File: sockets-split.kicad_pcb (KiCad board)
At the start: 2 copper layers, 63 parts, among them J2 MJ-4PP-9, P1 i2c-pin, P2 i2c-pin, SW1 RESET_SW, SW10 SW_PUSH, SW11 SW_PUSH, SW12 SW_PUSH, SW13 SW_PUSH, SW14 SW_PUSH, SW15 SW_PUSH, SW16 SW_PUSH, SW17 SW_PUSH, SW18 SW_PUSH, SW19 SW_PUSH, SW2 SW_PUSH, SW20 SW_PUSH, SW21 SW_PUSH, SW22 SW_PUSH, SW23 SW_PUSH, SW24 SW_PUSH, SW25 SW_PUSH, SW3 SW_PUSH, SW4 SW_PUSH, SW5 SW_PUSH, SW6 SW_PUSH, SW7 SW_PUSH, SW8 SW_PUSH, SW9 SW_PUSH, U1 ProMicro

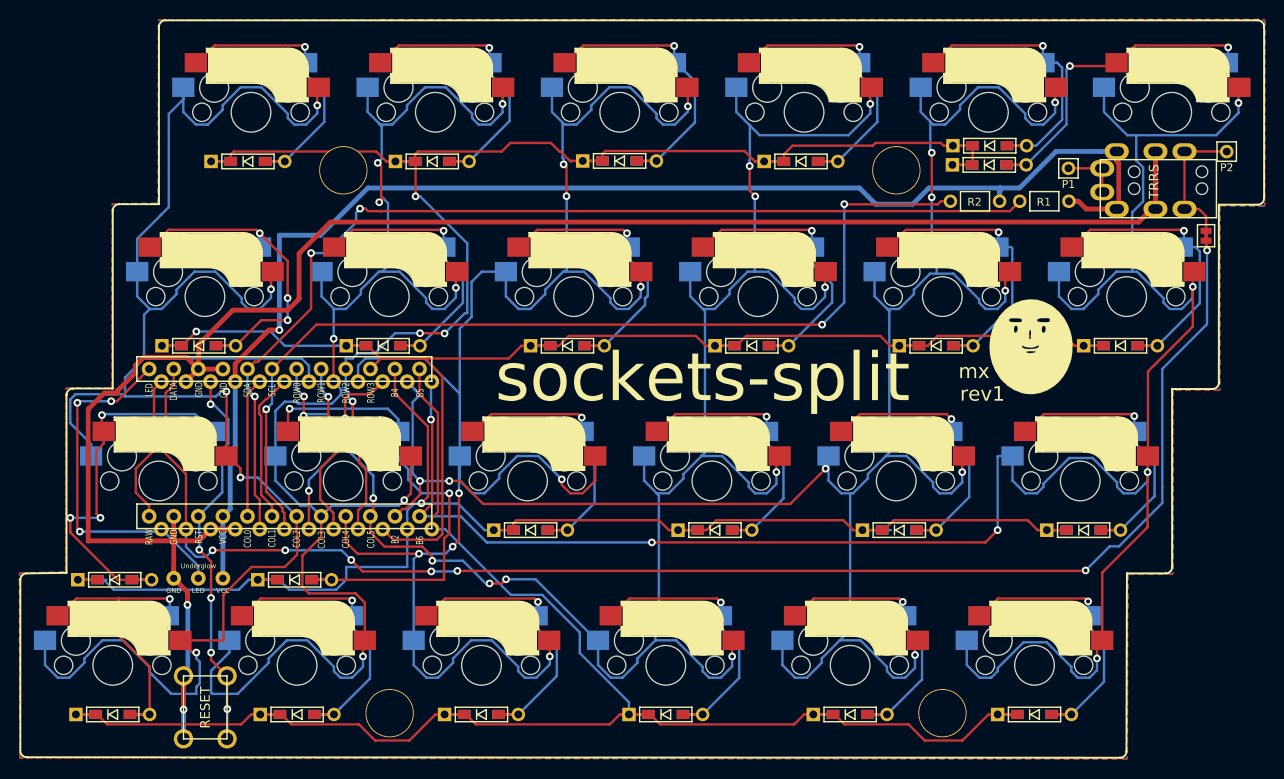
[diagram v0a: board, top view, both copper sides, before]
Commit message: Fix module & draw case line
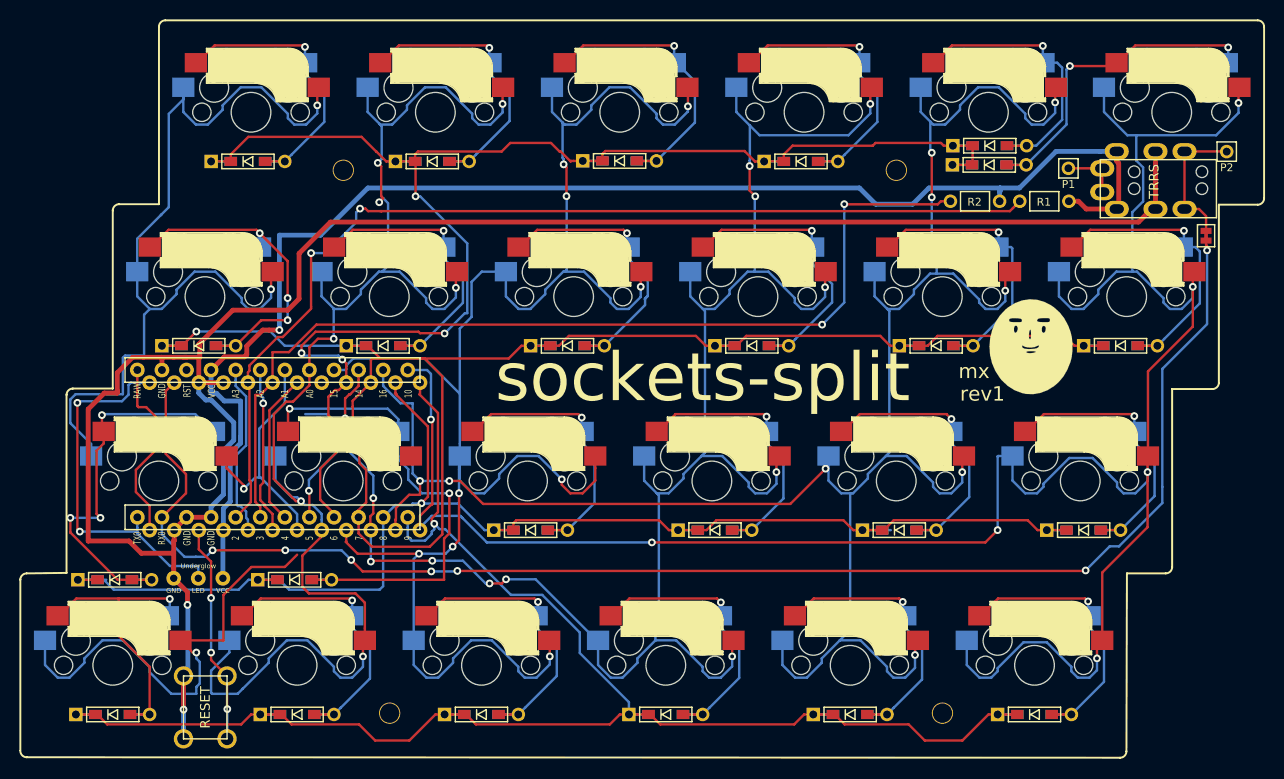
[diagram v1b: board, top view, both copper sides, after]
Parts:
- removed Ref** (x4): Val**, kbd:HOLE
- added ?: , kbd:HOLE_M2, F.Cu at (124.4, 67.8)
- added ?: , kbd:HOLE_M2, F.Cu at (181.9, 67.7)
- added ?: , kbd:HOLE_M2, F.Cu at (186.3, 124.1)
- added ?: , kbd:HOLE_M2, F.Cu at (129.4, 124.5)
- U1: footprint kbd:ProMicro_v2 -> kbd:ProMicro_v2_ura_pcb_for_sockets_split
- moved U1 1.22 mm to (117.6, 95.8)
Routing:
- net col0: track 191.0 -> 166.8 mm, vias 5 -> 4
- net row1: track 142.0 -> 164.6 mm
- net RESET: track 40.4 -> 22.8 mm, vias 5 -> 3
- net GND: track 189.3 -> 205.7 mm
- net row0: track 153.1 -> 163.4 mm
- net col1: track 158.5 -> 148.5 mm
- net VCC: track 142.8 -> 148.7 mm
- net col5: track 231.0 -> 236.7 mm
- net Net-(U1-Pad7): track 21.1 -> 15.8 mm, vias 3 -> 0
- net Net-(U1-Pad24): track 15.6 -> 20.4 mm
- net row3: track 164.4 -> 168.6 mm, vias 0 -> 1
- net col4: track 204.6 -> 208.8 mm
- net Net-(U1-Pad8): track 18.4 -> 14.5 mm
- net Net-(U1-Pad20): track 14.4 -> 18.0 mm
- net Net-(U1-Pad19): track 15.6 -> 17.3 mm, vias 0 -> 1
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- removed copper zone on B.Cu, net GND
- removed copper zone on F.Cu, net GND

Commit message: Fix promicro, case
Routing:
- net GND: track 205.7 -> 205.0 mm
- added copper zone on B.Cu, net GND
- added copper zone on F.Cu, net GND
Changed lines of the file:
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@@
     (thickness 1.6)
     (drawings 161)
-    (tracks 1485)
+    (tracks 1492)
     (zones 0)
     (modules 63)
@@
     (0 F.Cu signal)
     (31 B.Cu signal)
-    (32 B.Adhes user)
-    (33 F.Adhes user)
-    (34 B.Paste user)
-    (35 F.Paste user)
+    (32 B.Adhes user hide)
+    (33 F.Adhes user hide)
+    (34 B.Paste user hide)
+    (35 F.Paste user hide)
     (36 B.SilkS user)
     (37 F.SilkS user)
@@
     (39 F.Mask user)
     (40 Dwgs.User user)
-    (41 Cmts.User user)
-    (42 Eco1.User user)
-    (43 Eco2.User user)
-    (44 Edge.Cuts user)
-    (45 Margin user)
-    (46 B.CrtYd user)
+    (41 Cmts.User user hide)
+    (42 Eco1.User user hide)
+    (43 Eco2.User user hide)
+    (44 Edge.Cuts user hide)
+    (45 Margin user hide)
+    (46 B.CrtYd user hide)
     (47 F.CrtYd user hide)
-    (48 B.Fab user)
-    (49 F.Fab user)
+    (48 B.Fab user hide)
+    (49 F.Fab user hide)
   )
   (setup
@@
     (visible_elements 7FFFE7FF)
     (pcbplotparams
-      (layerselection 0x00100_7ffffffe)
+      (layerselection 0x010f0_ffffffff)
       (usegerberextensions false)
       (usegerberattributes false)
@@
       (padsonsilk false)
       (subtractmaskfromsilk false)
-      (outputformat 3)
+      (outputformat 1)
       (mirror false)
       (drillshape 0)
@@
   (segment (start 102.5622 109.7788) (end 104.5972 109.7788) (width 0.25) (layer B.Cu) (net 15))
   (segment (start 102.5622 109.7788) (end 104.5972 109.7788) (width 0.25) (layer F.Cu) (net 15))
-  (via (at 96.2014 103.378) (size 0.8) (drill 0.4) (layers F.Cu B.Cu) (net 15))
-  (segment (start 96.2014 104.894402) (end 96.2014 103.378) (width 0.25) (layer F.Cu) (net 15))
-  (via (at 99.314 103.378) (size 0.8) (drill 0.4) (layers F.Cu B.Cu) (net 15))
-  (segment (start 96.2014 103.378) (end 99.314 103.378) (width 0.25) (layer B.Cu) (net 15))
+  (via (at 97.3328 103.378) (size 0.8) (drill 0.4) (layers F.Cu B.Cu) (net 15))
+  (via (at 100.584 103.378) (size 0.8) (drill 0.4) (layers F.Cu B.Cu) (net 15))
+  (segment (start 97.4344 103.378) (end 100.547 103.378) (width 0.25) (layer B.Cu) (net 15))
   (segment (start 99.6465 95.698) (end 99.6465 94.448) (width 0.25) (layer F.Cu) (net 15))
   (segment (start 98.914001 96.430499) (end 99.6465 95.698) (width 0.25) (layer F.Cu) (net 15))
-  (segment (start 98.914001 102.978001) (end 98.914001 96.430499) (width 0.25) (layer F.Cu) (net 15))
-  (segment (start 99.314 103.378) (end 98.914001 102.978001) (width 0.25) (layer F.Cu) (net 15))
-  (segment (start 96.2014 104.894402) (end 96.207602 104.894402) (width 0.25) (layer F.Cu) (net 15))
   (segment (start 101.092 109.7788) (end 102.5622 109.7788) (width 0.25) (layer F.Cu) (net 15))
-  (segment (start 96.207602 104.894402) (end 101.092 109.7788) (width 0.25) (layer F.Cu) (net 15))
+  (segment (start 98.914001 100.5332) (end 99.472801 101.092) (width 0.25) (layer F.Cu) (net 15))
+  (segment (start 98.914001 100.5332) (end 98.914001 96.430499) (width 0.25) (layer F.Cu) (net 15))
+  (segment (start 99.472801 101.092) (end 100.0252 101.092) (width 0.25) (layer F.Cu) (net 15))
+  (segment (start 100.584 101.6508) (end 100.584 103.378) (width 0.25) (layer F.Cu) (net 15))
+  (segment (start 100.0252 101.092) (end 100.584 101.6508) (width 0.25) (layer F.Cu) (net 15))
+  (segment (start 97.3328 106.0196) (end 97.4344 106.1212) (width 0.25) (layer F.Cu) (net 15))
+  (segment (start 97.3328 103.378) (end 97.3328 106.0196) (width 0.25) (layer F.Cu) (net 15))
+  (segment (start 97.4344 106.1212) (end 101.092 109.7788) (width 0.25) (layer F.Cu) (net 15))
   (segment (start 96.9772 109.7788) (end 99.0122 109.7788) (width 0.25) (layer B.Cu) (net 16))
   (segment (start 115.57 109.7788) (end 117.605 109.7788) (width 0.25) (layer B.Cu) (net 16))
@@
   (segment (start 112.725199 96.723201) (end 112.8268 96.6216) (width 0.5) (layer B.Cu) (net 29))
   (via (at 96.9264 91.4908) (size 0.8) (drill 0.4) (layers F.Cu B.Cu) (net 30))
-  (via (at 97.1804 104.8004) (size 0.8) (drill 0.4) (layers F.Cu B.Cu) (net 30))
-  (segment (start 96.9264 91.4908) (end 96.9264 104.5464) (width 0.25) (layer F.Cu) (net 30))
-  (segment (start 96.9264 104.5464) (end 97.1804 104.8004) (width 0.25) (layer F.Cu) (net 30))
+  (via (at 98.3488 104.8004) (size 0.8) (drill 0.4) (layers F.Cu B.Cu) (net 30))
   (segment (start 109.4232 109.6264) (end 109.4232 108.3564) (width 0.25) (layer B.Cu) (net 30))
   (segment (start 103.124 104.39923) (end 103.124 104.8004) (width 0.25) (layer B.Cu) (net 30))
   (segment (start 103.124 103.3216) (end 103.124 104.39923) (width 0.25) (layer B.Cu) (net 30))
-  (segment (start 97.1804 104.8004) (end 103.124 104.8004) (width 0.25) (layer B.Cu) (net 30))
   (segment (start 106.493638 108.3564) (end 109.4232 108.3564) (width 0.25) (layer B.Cu) (net 30))
   (segment (start 103.124 104.986762) (end 106.493638 108.3564) (width 0.25) (layer B.Cu) (net 30))
@@
   (segment (start 96.9264 91.4908) (end 97.08804 91.32916) (width 0.25) (layer B.Cu) (net 30))
   (segment (start 97.08804 91.32916) (end 101.539168 91.32916) (width 0.25) (layer B.Cu) (net 30))
+  (segment (start 96.9264 101.3968) (end 97.282 101.3968) (width 0.25) (layer F.Cu) (net 30))
+  (segment (start 96.9264 91.4908) (end 96.9264 101.3968) (width 0.25) (layer F.Cu) (net 30))
+  (segment (start 98.3488 102.4636) (end 98.3488 104.8004) (width 0.25) (layer F.Cu) (net 30))
+  (segment (start 97.282 101.3968) (end 98.3488 102.4636) (width 0.25) (layer F.Cu) (net 30))
+  (segment (start 98.3488 104.8004) (end 103.124 104.8004) (width 0.25) (layer B.Cu) (net 30))
   (segment (start 111.9124 89.931762) (end 111.9124 89.17923) (width 0.5) (layer B.Cu) (net 31))
   (segment (start 208.8896 71.226601) (end 208.4488 71.667401) (width 0.5) (layer F.Cu) (net 31))
@@
   (segment (start 107.8992 126.209919) (end 107.893471 126.215648) (width 0.5) (layer B.Cu) (net 31))
   (segment (start 107.8992 123.19) (end 107.8992 126.209919) (width 0.5) (layer B.Cu) (net 31))
-  (segment (start 98.056197 105.758401) (end 98.046499 105.768099) (width 0.5) (layer F.Cu) (net 31))
-  (segment (start 98.046499 105.768099) (end 98.046499 92.148701) (width 0.5) (layer F.Cu) (net 31))
   (segment (start 99.716041 90.479159) (end 101.050855 90.479159) (width 0.5) (layer F.Cu) (net 31))
   (segment (start 98.046499 92.148701) (end 99.716041 90.479159) (width 0.5) (layer F.Cu) (net 31))
@@
   (segment (start 110.744 102.24397) (end 112.025189 100.962781) (width 0.5) (layer B.Cu) (net 31))
   (segment (start 110.744 103.3216) (end 110.744 102.24397) (width 0.5) (layer B.Cu) (net 31))
-  (segment (start 98.046499 105.768099) (end 102.262899 105.768099) (width 0.5) (layer F.Cu) (net 31))
   (segment (start 103.5304 107.0356) (end 106.8832 107.0356) (width 0.5) (layer F.Cu) (net 31))
   (segment (start 102.262899 105.768099) (end 103.5304 107.0356) (width 0.5) (layer F.Cu) (net 31))
   (segment (start 106.8832 108.54877) (end 106.8832 107.0356) (width 0.5) (layer F.Cu) (net 31))
   (segment (start 106.8832 107.0356) (end 106.8832 105.758401) (width 0.5) (layer F.Cu) (net 31))
+  (segment (start 98.046499 100.9396) (end 98.2472 100.9396) (width 0.5) (layer F.Cu) (net 31))
+  (segment (start 98.046499 100.9396) (end 98.046499 92.148701) (width 0.5) (layer F.Cu) (net 31))
+  (segment (start 99.4156 102.108) (end 99.4156 105.768099) (width 0.5) (layer F.Cu) (net 31))
+  (segment (start 98.2472 100.9396) (end 99.4156 102.108) (width 0.5) (layer F.Cu) (net 31))
+  (segment (start 99.4156 105.768099) (end 102.262899 105.768099) (width 0.5) (layer F.Cu) (net 31))
   (via (at 110.8964 106.7308) (size 0.8) (drill 0.4) (layers F.Cu B.Cu) (net 32))
   (via (at 118.4148 106.7308) (size 0.8) (drill 0.4) (layers F.Cu B.Cu) (net 32))
@@
   (segment (start 212.834 71.464201) (end 213.5632 72.193401) (width 0.25) (layer F.Cu) (net 48))
   (segment (start 211.334 71.464201) (end 212.834 71.464201) (width 0.25) (layer F.Cu) (net 48))
+  (zone (net 31) (net_name GND) (layer F.Cu) (hatch edge 0.508)
+    (connect_pads (clearance 0.508))
+    (min_thickness 0.254)
+    (fill yes (arc_segments 16) (thermal_gap 0.508) (thermal_bridge_width 0.508))
+    (polygon
+      (pts
+        (xy 105.3592 52.0192) (xy 105.3592 70.9168) (xy 100.5332 71.0184) (xy 100.5332 89.9668) (xy 95.8596 90.0176)
+        (xy 95.758 109.0676) (xy 91.0844 109.1184) (xy 91.0336 128.1684) (xy 205.3336 128.1684) (xy 205.3844 109.1184)
+        (xy 210.058 109.1184) (xy 210.1088 90.0684) (xy 214.884 90.0176) (xy 214.9348 71.0184) (xy 219.5068 70.9676)
+        (xy 219.456 51.9684)
+      )
+    )
+  )
+  (zone (net 31) (net_name GND) (layer B.Cu) (hatch edge 0.508)
+    (connect_pads (clearance 0.508))
+    (min_thickness 0.254)
+    (fill yes (arc_segments 16) (thermal_gap 0.508) (thermal_bridge_width 0.508))
+    (polygon
+      (pts
+        (xy 105.3592 52.0192) (xy 105.3592 70.9168) (xy 100.5332 71.0184) (xy 100.5332 89.9668) (xy 95.8596 90.0176)
+        (xy 95.758 109.0676) (xy 91.0844 109.1184) (xy 91.0336 128.1684) (xy 205.3336 128.1684) (xy 205.3844 109.1184)
+        (xy 210.058 109.1184) (xy 210.1088 90.0684) (xy 214.884 90.0176) (xy 214.9348 71.0184) (xy 219.5068 70.9676)
+        (xy 219.456 51.9684)
+      )
+    )
+  )
 )
